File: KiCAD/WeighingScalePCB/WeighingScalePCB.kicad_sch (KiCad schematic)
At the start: 48 parts, among them IC1 MAX6675ISA+T, IC2 APS11753KMDALX-9PL5, IC3 CAP1203-1-SN, J1 Conn_01x14_MountingPin, J2 AudioJack4, J4 Battery Conn, J6 Conn_01x04_MountingPin, Q2 NX138AKR, Q3 NX138AKR, Q5 NX138AKR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

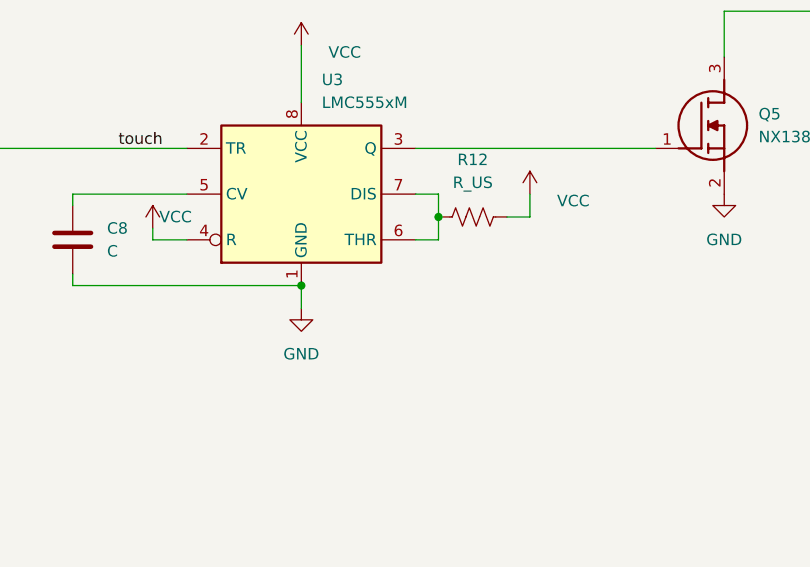
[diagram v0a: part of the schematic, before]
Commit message: added cap to threshold of 555, design 555 timer and simulate with next commit
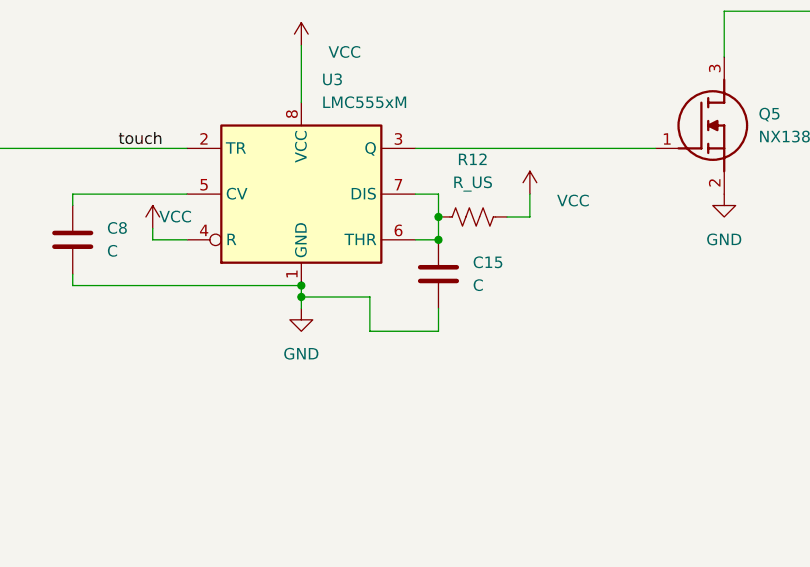
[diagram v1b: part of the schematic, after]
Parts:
- added C15: C, symbol Device:C
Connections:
- net GND: now also C15.2
- net at R12.1, U3.6 (THR), U3.7 (DIS): now also C15.1
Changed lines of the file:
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@@
 	)
 	(junction
+		(at 302.26 191.77)
+		(diameter 0)
+		(color 0 0 0 0)
+	)
+	(junction
 		(at 76.2 200.66)
 		(diameter 0)
@@
 		(color 0 0 0 0)
 	)
+	(junction
+		(at 287.02 198.12)
+		(diameter 0)
+		(color 0 0 0 0)
+	)
 	(no_connect
 		(at 113.03 58.42)
@@
 	(wire
 		(pts
+			(xy 302.26 199.39) (xy 302.26 201.93)
+		)
+		(stroke
+			(width 0)
+			(type default)
+		)
+	)
+	(wire
+		(pts
 			(xy 363.22 107.95) (xy 360.68 107.95)
 		)
@@
 	(wire
 		(pts
-			(xy 287.02 196.85) (xy 287.02 199.39)
+			(xy 287.02 196.85) (xy 287.02 198.12)
 		)
 		(stroke
@@
 	(wire
 		(pts
+			(xy 302.26 201.93) (xy 294.64 201.93)
+		)
+		(stroke
+			(width 0)
+			(type default)
+		)
+	)
+	(wire
+		(pts
 			(xy 83.82 137.16) (xy 83.82 144.78)
 		)
@@
 	(wire
 		(pts
+			(xy 294.64 198.12) (xy 287.02 198.12)
+		)
+		(stroke
+			(width 0)
+			(type default)
+		)
+	)
+	(wire
+		(pts
 			(xy 63.5 73.66) (xy 63.5 74.93)
 		)
@@
 	(wire
 		(pts
+			(xy 287.02 198.12) (xy 287.02 199.39)
+		)
+		(stroke
+			(width 0)
+			(type default)
+		)
+	)
+	(wire
+		(pts
 			(xy 38.1 165.1) (xy 44.45 165.1)
 		)
@@
 	(wire
 		(pts
+			(xy 294.64 201.93) (xy 294.64 198.12)
+		)
+		(stroke
+			(width 0)
+			(type default)
+		)
+	)
+	(wire
+		(pts
 			(xy 270.51 191.77) (xy 270.51 190.5)
 		)
@@
 					(unit 1)
 				)
+			)
+		)
+	)
+	(symbol
+		(lib_id "Device:C")
+		(at 302.26 195.58 0)
+		(unit 1)
+		(exclude_from_sim no)
+		(in_bom yes)
+		(on_board yes)
+		(dnp no)
+		(fields_autoplaced yes)
+		(property "Reference" "C15"
+			(at 306.07 194.3099 0)
+			(effects
+				(font
+					(size 1.27 1.27)
+				)
+				(justify left)
+			)
+		)
+		(property "Value" "C"
+			(at 306.07 196.8499 0)
+			(effects
+				(font
+					(size 1.27 1.27)
+				)
+				(justify left)
+			)
+		)
+		(property "Footprint" ""
+			(at 303.2252 199.39 0)
+			(effects
+				(font
+					(size 1.27 1.27)
+				)
+				(hide yes)
+			)
+		)
+		(property "Datasheet" "~"
+			(at 302.26 195.58 0)
+			(effects
+				(font
+					(size 1.27 1.27)
+				)
+				(hide yes)
+			)
+		)
+		(property "Description" "Unpolarized capacitor"
+			(at 302.26 195.58 0)
+			(effects
+				(font
+					(size 1.27 1.27)
+				)
+				(hide yes)
+			)
+		)
+		(pin "2"
+		)
+		(pin "1"
+		)
+		(instances
+			(project "WeighingScalePCB"
+				(path "/fb3b7c1c-1dc1-4229-b305-25c6e0b4dbdc"
+					(reference "C15")
+					(unit 1)
+				)

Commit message: DRCs cleared
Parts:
- removed Q2, Q3: NX138AKR, Footprints:SOT95P230X110-3N, symbol NX138AKR Mosfet:NX138AKR
- removed R10: 1K, Resistor_SMD:R_0603_1608Metric, symbol Device:R_US
- removed R11: 5K, Resistor_SMD:R_0603_1608Metric, symbol Device:R_US
- added R13: 220k, Resistor_SMD:R_0603_1608Metric, symbol Device:R_US
- added U4: 74LVC1G32, Footprints:SOT95P285X140-5N, symbol 74xGxx:74LVC1G32
- C10, C11: value C -> 0.1u; footprint (none) -> Capacitor_SMD:C_0603_1608Metric
- C15: value C -> 10u; footprint (none) -> Capacitor_SMD:C_0603_1608Metric
- C8: value C -> 0.01u; footprint (none) -> Capacitor_SMD:C_0603_1608Metric
- C9: value C -> 1u; footprint (none) -> Capacitor_SMD:C_0603_1608Metric
- IC3: footprint SOIC127P600X175-8N -> Footprints:CAP1203_SOIC127P600X175-8N
- R12: value R_US -> 47k; footprint (none) -> Resistor_SMD:R_0603_1608Metric
- R4: value 10K -> 10k
- R7, R8: value 10K -> 4.7k
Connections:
- net GND: now also U4.3 (GND); no longer J6.4 (Pin_4), R1.1
- net VCC: now also R13.2; no longer BZ1.1 (+)
- net V_BAT: now also U4.5 (VCC)
- net ble_keep_awake: now also U4.2
- net enable: now also U1.4 (GPIO21_D3), U4.4; no longer U1.19 (CHIP_EN)
- net touch: now also U1.11 (GPIO18_D10_MOSI); no longer U1.4 (GPIO21_D3)
- net at IC2.2 (VOUT): now also U4.1
- net at IC3.7 (CS2): now also T1.T1 (Pad); no longer T2.T2 (Pad)
- net at IC3.8 (CS1): now also T2.T2 (Pad); no longer T1.T1 (Pad)
- net load_P: now reaches J6.3 (Pin_3), R2.1
- new net: BZ1.1 (+), R13.1
- new net load_N: J6.4 (Pin_4), R1.1
- no-connect marks 14 -> 16
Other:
- moved on the sheet: IC2
